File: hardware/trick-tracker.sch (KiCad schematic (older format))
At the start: 53 parts, among them J1 USB4105-GF-A, J2 S2B-PH-K, J3 QWiiC, J4 MEM2051-00-195-00-A, J5 Debug, J6 QWiiC, P1 SMTB-1240-S-R, U1 MS88SF2, U2 DPS368XTSA1, U3 LSM9DS1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

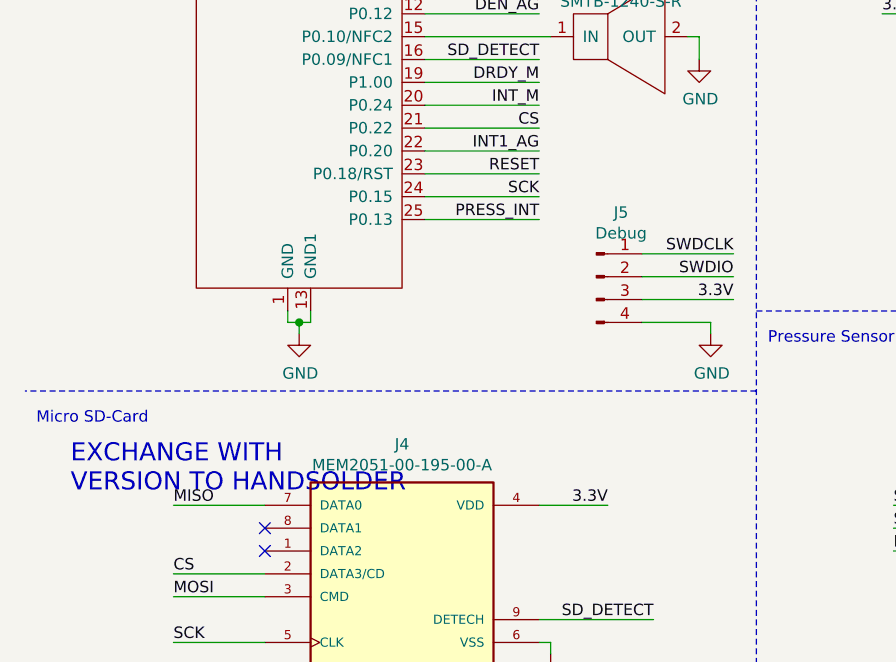
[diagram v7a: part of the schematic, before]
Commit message: Exchanged SD Card holder with one which can be hand-soldered
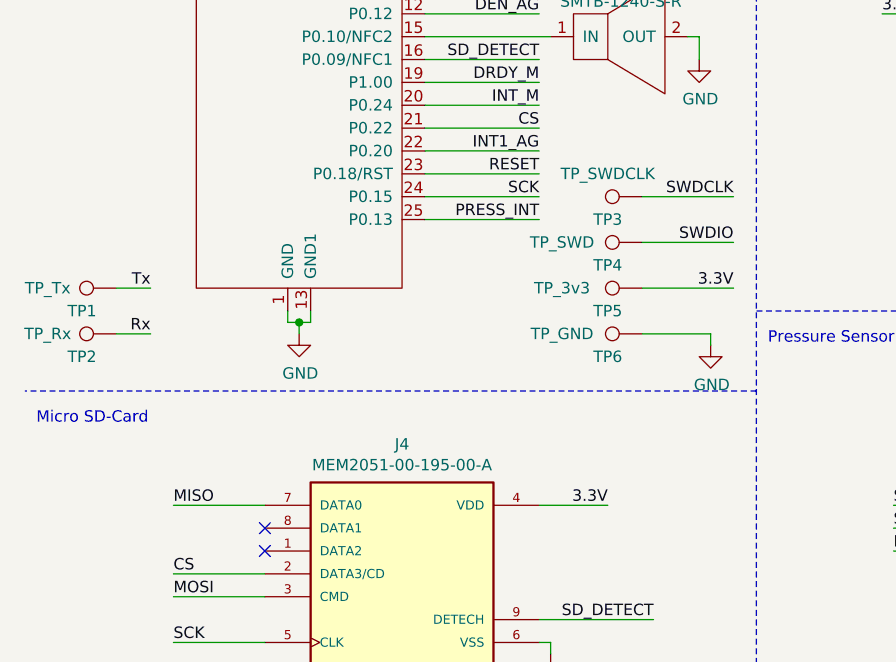
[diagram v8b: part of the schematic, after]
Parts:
- removed J5: Debug, Connector_PinSocket_2.54mm:PinSocket_1x04_P2.54mm_Vertical, symbol Connector:Conn_01x04_Male
- added TP1: TP_Tx, TestPoint:TestPoint_Pad_D1.5mm, symbol Connector:TestPoint
- added TP2: TP_Rx, TestPoint:TestPoint_Pad_D1.5mm, symbol Connector:TestPoint
- added TP3: TP_SWDCLK, TestPoint:TestPoint_Pad_D1.5mm, symbol Connector:TestPoint
- added TP4: TP_SWD, TestPoint:TestPoint_Pad_D1.5mm, symbol Connector:TestPoint
- added TP5: TP_3v3, TestPoint:TestPoint_Pad_D1.5mm, symbol Connector:TestPoint
- added TP6: TP_GND, TestPoint:TestPoint_Pad_D1.5mm, symbol Connector:TestPoint
- J4: footprint MEM2051-00-195-00-A:GCT_MEM2051-00-195-00-A -> MEM2061-01-188-00-A_REVA:GCT_MEM2061-01-188-00-A_REVA
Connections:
- net 3.3V: now also TP5.1
- net GND: now also TP6.1
- net Rx: now also TP2.1
- net SWDCLK: now also TP3.1
- net SWDIO: now also TP4.1
- net Tx: now also TP1.1
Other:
- note removed: "EXCHANGE WITH \nVERSION TO HANDSOLDER"
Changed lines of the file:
@@
 F 0 "J4" H 2150 5067 50  0000 C CNN
 F 1 "MEM2051-00-195-00-A" H 2150 4976 50  0000 C CNN
-F 2 "MEM2051-00-195-00-A:GCT_MEM2051-00-195-00-A" H 2150 4500 50  0001 L BNN
+F 2 "MEM2061-01-188-00-A_REVA:GCT_MEM2061-01-188-00-A_REVA" H 2150 4500 50  0001 L BNN
 F 3 "" H 2150 4500 50  0001 L BNN
 F 4 "GCT" H 2150 4500 50  0001 L BNN "MANUFACTURER"
@@
 Text Notes 550  600  0    50   ~ 0
 MCU
-$Comp
-L Connector:Conn_01x04_Male J5
-U 1 1 60AB9726
-P 3000 3200
-F 0 "J5" H 3108 3481 50  0000 C CNN
-F 1 "Debug" H 3108 3390 50  0000 C CNN
-F 2 "Connector_PinSocket_2.54mm:PinSocket_1x04_P2.54mm_Vertical" H 3000 3200 50  0001 C CNN
-F 3 "~" H 3000 3200 50  0001 C CNN
-	1    3000 3200
-	1    0    0    -1
-$EndComp
-Text Label 3600 3100 2    50   ~ 0
+Text Label 3600 2850 2    50   ~ 0
 SWDCLK
-Text Label 3600 3200 2    50   ~ 0
+Text Label 3600 3050 2    50   ~ 0
 SWDIO
 $Comp
 L power:GND #PWR0132
 U 1 1 60AB9E9C
-P 3500 3450
-F 0 "#PWR0132" H 3500 3200 50  0001 C CNN
-F 1 "GND" H 3505 3277 50  0000 C CNN
-F 2 "" H 3500 3450 50  0001 C CNN
-F 3 "" H 3500 3450 50  0001 C CNN
-	1    3500 3450
-	1    0    0    -1
-$EndComp
-Text Label 3600 3300 2    50   ~ 0
+P 3500 3500
+F 0 "#PWR0132" H 3500 3250 50  0001 C CNN
+F 1 "GND" H 3505 3327 50  0000 C CNN
+F 2 "" H 3500 3500 50  0001 C CNN
+F 3 "" H 3500 3500 50  0001 C CNN
+	1    3500 3500
+	1    0    0    -1
+$EndComp
+Text Label 3600 3250 2    50   ~ 0
 3.3V
 Wire Wire Line
-	3200 3100 3600 3100
-Wire Wire Line
-	3600 3200 3200 3200
-Wire Wire Line
-	3200 3300 3600 3300
-Wire Wire Line
-	3500 3450 3500 3400
-Wire Wire Line
-	3500 3400 3200 3400
+	3200 2850 3600 2850
+Wire Wire Line
+	3600 3050 3200 3050
+Wire Wire Line
+	3200 3250 3600 3250
+Wire Wire Line
+	3500 3500 3500 3450
+Wire Wire Line
+	3500 3450 3200 3450
 $Comp
 L SMTB-1240-S-R:SMTB-1240-S-R P1
@@
 NoConn ~ 2800 7250
 NoConn ~ 1950 7250
-Text Notes 700  4150 0    79   ~ 0
-EXCHANGE WITH \nVERSION TO HANDSOLDER
+$Comp
+L Connector:TestPoint TP3
+U 1 1 60ADEE00
+P 3200 2850
+F 0 "TP3" V 3100 3000 50  0000 C CNN
+F 1 "TP_SWDCLK" V 3300 3000 50  0000 C CNN
+F 2 "TestPoint:TestPoint_Pad_D1.5mm" H 3400 2850 50  0001 C CNN
+F 3 "~" H 3400 2850 50  0001 C CNN
+	1    3200 2850
+	0    -1   -1   0
+$EndComp
+$Comp
+L Connector:TestPoint TP4
+U 1 1 60ADFAD3
+P 3200 3050
+F 0 "TP4" V 3100 3200 50  0000 C CNN
+F 1 "TP_SWD" V 3200 3400 50  0000 C CNN
+F 2 "TestPoint:TestPoint_Pad_D1.5mm" H 3400 3050 50  0001 C CNN
+F 3 "~" H 3400 3050 50  0001 C CNN
+	1    3200 3050
+	0    -1   -1   0
+$EndComp
+$Comp
+L Connector:TestPoint TP5
+U 1 1 60ADFC18
+P 3200 3250
+F 0 "TP5" V 3100 3400 50  0000 C CNN
+F 1 "TP_3v3" V 3200 3600 50  0000 C CNN
+F 2 "TestPoint:TestPoint_Pad_D1.5mm" H 3400 3250 50  0001 C CNN
+F 3 "~" H 3400 3250 50  0001 C CNN
+	1    3200 3250
+	0    -1   -1   0
+$EndComp
+$Comp
+L Connector:TestPoint TP6
+U 1 1 60ADFDB3
+P 3200 3450
+F 0 "TP6" V 3100 3600 50  0000 C CNN
+F 1 "TP_GND" V 3200 3800 50  0000 C CNN
+F 2 "TestPoint:TestPoint_Pad_D1.5mm" H 3400 3450 50  0001 C CNN
+F 3 "~" H 3400 3450 50  0001 C CNN
+	1    3200 3450
+	0    -1   -1   0
+$EndComp
+$Comp
+L Connector:TestPoint TP1
+U 1 1 60B93083
+P 900 3250
+F 0 "TP1" V 800 3400 50  0000 C CNN
+F 1 "TP_Tx" V 900 3550 50  0000 C CNN
+F 2 "TestPoint:TestPoint_Pad_D1.5mm" H 1100 3250 50  0001 C CNN
+F 3 "~" H 1100 3250 50  0001 C CNN
+	1    900  3250
+	0    -1   -1   0
+$EndComp
+$Comp
+L Connector:TestPoint TP2
+U 1 1 60B93507
+P 900 3450
+F 0 "TP2" V 800 3600 50  0000 C CNN
+F 1 "TP_Rx" V 900 3750 50  0000 C CNN
+F 2 "TestPoint:TestPoint_Pad_D1.5mm" H 1100 3450 50  0001 C CNN
+F 3 "~" H 1100 3450 50  0001 C CNN
+	1    900  3450
+	0    -1   -1   0
+$EndComp
+Text Label 1050 3450 2    50   ~ 0
+Rx
+Text Label 1050 3250 2    50   ~ 0
+Tx
+Wire Wire Line
+	1050 3250 900  3250
+Wire Wire Line
+	1050 3450 900  3450
 $EndSCHEMATC
